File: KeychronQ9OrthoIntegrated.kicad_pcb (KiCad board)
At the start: 2 copper layers, 309.6 x 76.2 mm, 168 parts, among them J1 Conn_01x07, J3 Conn_01x05, SW1 RotaryEncoder_Switch, SW2 RotaryEncoder_Switch, U1 XC6206PxxxMR, U2 SRV05-4, U3 RP2040, U4 W25Q128JVS, Y1 Crystal_GND24

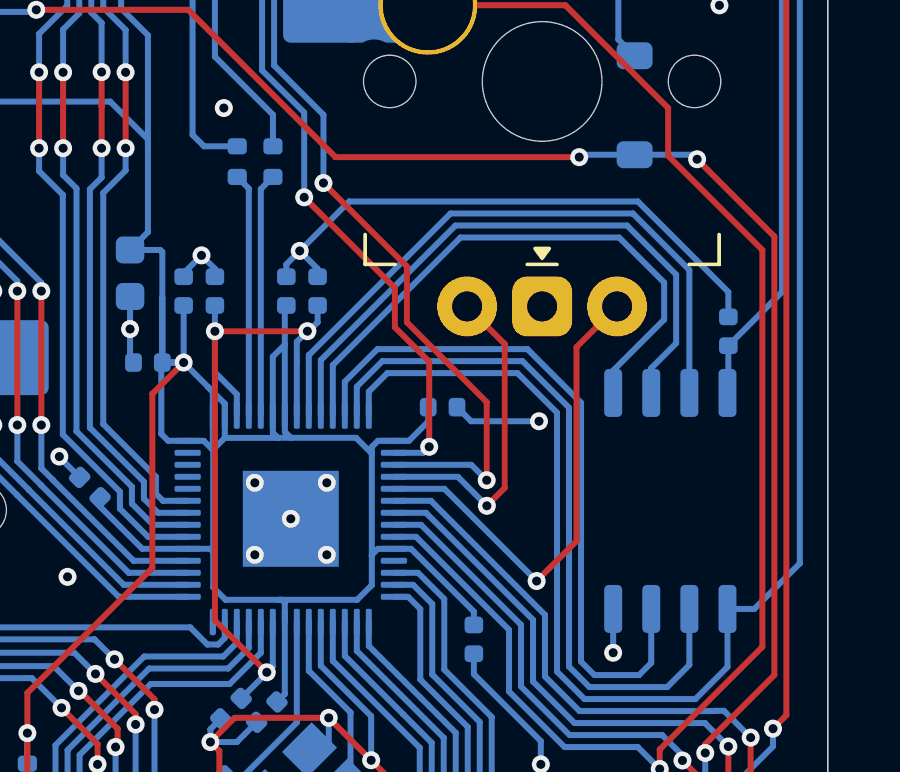
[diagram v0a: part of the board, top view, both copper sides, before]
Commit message: route vias away from top case resting point
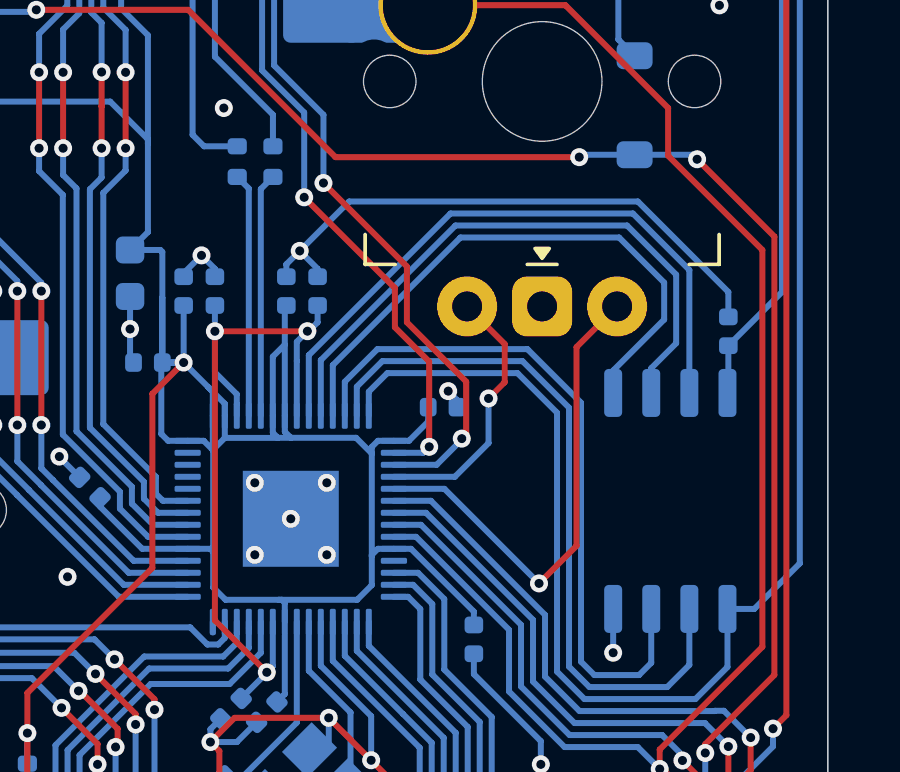
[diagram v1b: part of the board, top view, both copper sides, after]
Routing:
- net GND: track 110.2 -> 108.0 mm
- net ENC1A: track 39.3 -> 37.1 mm
- net ENC2A: track 10.9 -> 8.92 mm
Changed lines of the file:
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@@
 	)
 	(via
-		(at 315.808328 60.539705)
+		(at 312.780654 59.535888)
 		(size 0.6)
 		(drill 0.3)
@@
 	)
 	(segment
+		(start 313.07466 59.829894)
+		(end 313.07466 60.070652)
+		(width 0.2)
+		(layer "B.Cu")
+		(net 2)
+	)
+	(segment
 		(start 302.1767 57.466162)
 		(end 302.1767 56.380812)
@@
 	)
 	(segment
+		(start 312.780654 59.535888)
+		(end 313.07466 59.829894)
+		(width 0.2)
+		(layer "B.Cu")
+		(net 2)
+	)
+	(segment
 		(start 307.804215 74.248718)
 		(end 307.132128 74.248718)
@@
 	)
 	(segment
-		(start 313.543713 60.539705)
-		(end 313.07466 60.070652)
-		(width 0.2)
-		(layer "B.Cu")
-		(net 2)
-	)
-	(segment
 		(start 307.645036 76.254604)
 		(end 306.385639 74.995207)
@@
 	)
 	(segment
-		(start 315.808328 60.539705)
-		(end 313.543713 60.539705)
-		(width 0.2)
-		(layer "B.Cu")
-		(net 2)
-	)
-	(segment
 		(start 283.7125 48.557964)
 		(end 283.7125 49.000349)
@@
 	)
 	(segment
-		(start 314.065084 59.903968)
-		(end 314.065084 62.50482)
+		(start 311.404036 55.379386)
+		(end 308.622795 52.598145)
 		(width 0.2)
 		(layer "F.Cu")
@@
 	(segment
 		(start 311.404036 57.24292)
-		(end 314.065084 59.903968)
+		(end 311.404036 55.379386)
 		(width 0.2)
 		(layer "F.Cu")
@@
 	)
 	(segment
-		(start 311.404036 55.379386)
+		(start 313.382172 59.221056)
 		(end 311.404036 57.24292)
 		(width 0.2)
@@
 	)
 	(segment
-		(start 308.622795 52.598145)
-		(end 311.404036 55.379386)
+		(start 313.382172 60.969884)
+		(end 313.382172 59.221056)
+		(width 0.2)
+		(layer "F.Cu")
+		(net 115)
+	)
+	(segment
+		(start 313.233344 61.118712)
+		(end 313.382172 60.969884)
 		(width 0.2)
 		(layer "F.Cu")
@@
 	)
 	(via
-		(at 314.065084 62.50482)
+		(at 313.233344 61.118712)
 		(size 0.6)
 		(drill 0.3)
@@
 	)
 	(segment
-		(start 314.065084 62.50482)
-		(end 313.551616 61.991352)
+		(start 313.233344 61.154713)
+		(end 312.396705 61.991352)
 		(width 0.2)
 		(layer "B.Cu")
@@
 	)
 	(segment
-		(start 313.551616 61.991352)
-		(end 310.972008 61.991352)
+		(start 313.233344 61.118712)
+		(end 313.233344 61.154713)
 		(width 0.2)
 		(layer "B.Cu")
@@
 	)
 	(segment
+		(start 312.396705 61.991352)
+		(end 310.972008 61.991352)
+		(width 0.2)
+		(layer "B.Cu")
+		(net 115)
+	)
+	(segment
 		(start 308.622795 52.598145)
 		(end 308.622795 50.324121)
@@
 	)
 	(segment
-		(start 317.0595 58.0655)
-		(end 318.4125 56.7125)
+		(start 315.808328 65.945125)
+		(end 317.0595 64.693953)
 		(width 0.2)
 		(layer "F.Cu")
@@
 	)
 	(segment
-		(start 317.0595 64.535492)
+		(start 317.0595 64.693953)
 		(end 317.0595 58.0655)
 		(width 0.2)
@@
 	)
 	(segment
-		(start 315.729099 65.865893)
-		(end 317.0595 64.535492)
+		(start 317.0595 58.0655)
+		(end 318.4125 56.7125)
 		(width 0.2)
 		(layer "F.Cu")
@@
 	)
 	(via
-		(at 315.729099 65.865893)
+		(at 315.808328 65.945125)
 		(size 0.6)
 		(drill 0.3)
@@
 	)
 	(segment
-		(start 315.729099 65.865893)
+		(start 315.808328 65.945122)
 		(end 312.654558 62.791352)
 		(width 0.2)
@@
 	)
 	(segment
-		(start 314.665084 62.762724)
+		(start 315.808328 65.945125)
+		(end 315.808328 65.945122)
+		(width 0.2)
+		(layer "B.Cu")
+		(net 116)
+	)
+	(segment
+		(start 314.665084 59.240488)
 		(end 314.665084 57.965084)
 		(width 0.2)
@@
 	)
 	(segment
-		(start 314.069772 63.358036)
-		(end 314.665084 62.762724)
+		(start 314.126312 59.77926)
+		(end 314.665084 59.240488)
 		(width 0.2)
 		(layer "F.Cu")
@@
 	)
 	(via
-		(at 314.069772 63.358036)
+		(at 314.126312 59.77926)
 		(size 0.6)
 		(drill 0.3)
@@
 	)
 	(segment
-		(start 313.103088 62.391352)
-		(end 310.972008 62.391352)
+		(start 314.126312 61.26754)
+		(end 313.0025 62.391352)
 		(width 0.2)
 		(layer "B.Cu")
@@
 	)
 	(segment
-		(start 314.069772 63.358036)
-		(end 313.103088 62.391352)
+		(start 314.126312 59.77926)
+		(end 314.126312 61.26754)
+		(width 0.2)
+		(layer "B.Cu")
+		(net 117)
+	)
+	(segment
+		(start 313.0025 62.391352)
+		(end 310.972008 62.391352)
 		(width 0.2)
 		(layer "B.Cu")

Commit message: add spacebar for 3u center cluster
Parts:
- added MX68: MX_SW_HS, PCM_marbastlib-mx:SW_MX_HS_S_CPG151101S11_1u, B.Cu at (206.4, 82.5)
- added S5: MX_stab, PCM_marbastlib-mx:STAB_MX_P_2u, B.Cu at (206.4, 82.5)
- MX58: footprint PCM_marbastlib-mx:SW_MX_HS_CPG151101S11_1u -> PCM_marbastlib-mx:SW_MX_HS_S_CPG151101S11_1u
- moved D59 9.43 mm to (221.1, 80.5), turned to 180 degrees
- moved D58 6.13 mm to (194.5, 86.1), turned to 0 degrees
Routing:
- net Row 4: track 341.4 -> 397.5 mm, vias 10 -> 8
- net Col 10: track 199.9 -> 220.7 mm, vias 4 -> 5
- net Net-(D58-A): track 4.45 -> 22.3 mm
- net Col 11: track 207.4 -> 201.9 mm
- net GND: track 108.0 -> 113.1 mm, vias 75 -> 81
- net Net-(D59-A): track 16.6 -> 12.2 mm
- net ENC1B: track 42.2 -> 45.2 mm
- net Col 13: track 166.3 -> 167.4 mm
- net Q_CLK: track 20.5 -> 21.2 mm
- net Q_IO3: track 21.5 -> 22.3 mm
- net Q_IO0: track 19.5 -> 20.2 mm
- net Q_IO1: track 24.1 -> 23.5 mm
- net Q_SEL: track 55.1 -> 54.4 mm
- net Q_IO2: track 23.3 -> 22.7 mm
- net ENC2A: track 8.92 -> 8.38 mm
